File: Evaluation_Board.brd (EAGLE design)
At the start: 60.9 x 39.4 mm, 41 parts, among them IC1 MEGA32-A, IC2 FT232RL, IC3 317EMP, J1 DCJ0202

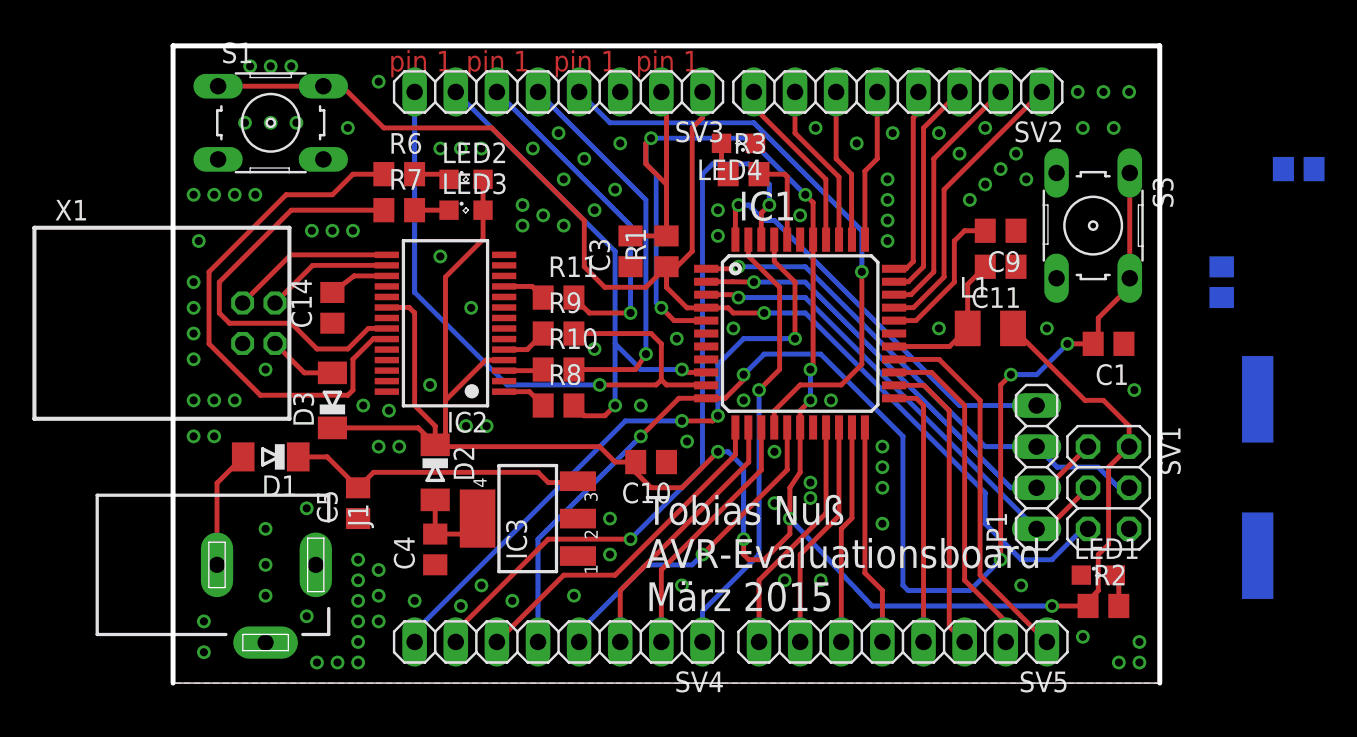
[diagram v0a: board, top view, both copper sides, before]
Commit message: Quarz eingefügt
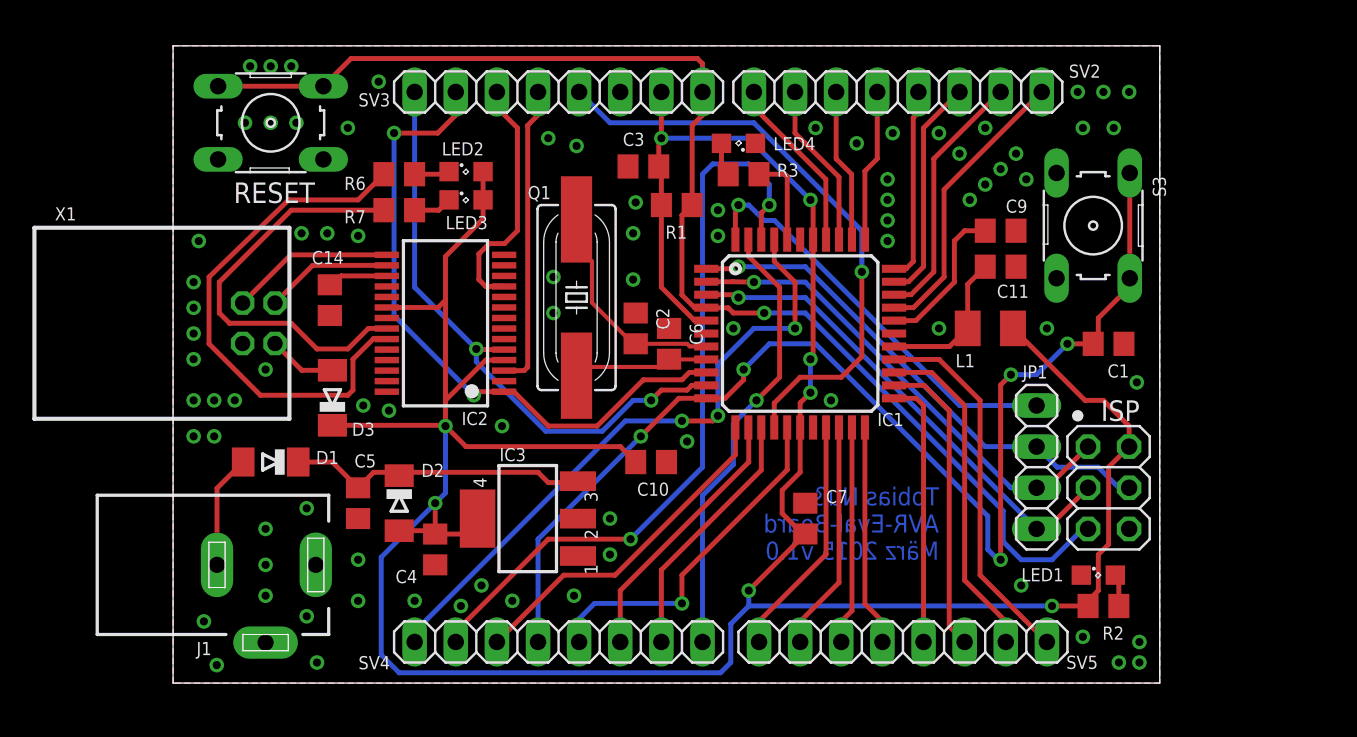
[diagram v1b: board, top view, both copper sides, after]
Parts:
- removed R10, R11, R8, R9: 1k, rcl:R0805
- added C7: 100n, rcl:C0805
- C2, C6: value 100n -> 12p
- Q1: value (none) -> 16 MHz
- moved Q1 43.5 mm to (24.9, 23.8), flipped to the top
- moved C6 40.4 mm to (30.6, 21.0), flipped to the top, turned to 270 degrees
- moved C2 36.3 mm to (28.6, 21.9), flipped to the top
- moved C3 5.30 mm to (29.1, 31.9), turned to 0 degrees
- moved D2 2.93 mm to (14.0, 11.1)
- moved R1 2.93 mm to (31.1, 29.5), turned to 180 degrees
- moved LED3 0.63 mm to (18.1, 29.8)
- moved C14 0.50 mm to (9.68, 23.7)
- moved LED2 0.48 mm to (18.1, 31.6)
- moved D1 0.32 mm to (6.03, 13.7)
- moved D3 0.16 mm to (9.84, 17.6)
- renumbered S1 to RESET, SV1 to ISP
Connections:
- removed net N$2: C4.2, D2.A, IC3.4
- removed net N$21: IC2.1, R8.1
- removed net N$22: IC2.5, R9.1
- removed net N$23: IC2.3, R10.1
- removed net N$24: IC2.11, R11.1
- new net N$17: C2.2, IC1.7, Q1.2
- new net N$25: C6.2, IC1.8, Q1.1
- net +5V: now also C4.2, C7.2, D2.A, IC3.4; no longer D2.C
- net CTS: now also IC2.11; no longer R11.2
- net GND: now also C2.1, C6.1, C7.1
- net NETZ: now also D2.C
- net RTS: now also IC2.3; no longer R10.2
- net RX_USB: now also IC2.1; no longer R8.2
- net TX_USB: now also IC2.5; no longer R9.2
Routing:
- net +5V: track 174.9 -> 191.8 mm, vias 9 -> 8
- net N$17: track 0.00 -> 13.9 mm
- net N$25: track 0.00 -> 8.82 mm
- net RX_USB: track 32.9 -> 40.6 mm
- net CTS: track 21.0 -> 15.4 mm, vias 1 -> 0
- net N$2: track 5.12 -> 0.00 mm
- net RTS: track 23.9 -> 18.8 mm, vias 1 -> 0
- net PD2_INT0: track 81.1 -> 76.1 mm
- net RESET: track 83.3 -> 79.3 mm
- net TX_USB: track 40.9 -> 37.4 mm, vias 1 -> 2
- net N$22: track 2.82 -> 0.00 mm
- net N$21: track 2.76 -> 0.00 mm
- net N$24: track 2.69 -> 0.00 mm
- net N$23: track 2.44 -> 0.00 mm
- net OC2: track 20.2 -> 21.7 mm
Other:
- board text added: "Tobias Nuß AVR-Eval-Board März 2015 v1.0"
- board text removed: "Tobias Nuß AVR-Evaluationsboard März 2015"
- board text removed: "pin 1"

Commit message: Test mit einem neuen Branch namens edit.
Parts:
- removed C7: 100n, rcl:C0805
- added R10, R11, R8, R9: 1k, rcl:R0805
- C2, C6: value 12p -> 100n
- Q1: value 16 MHz -> (none)
- moved Q1 43.5 mm to (67.0, 12.7), flipped to the bottom
- moved C6 40.4 mm to (69.5, 31.8), flipped to the bottom, turned to 180 degrees
- moved C2 36.3 mm to (64.8, 24.8), flipped to the bottom
- moved C3 5.30 mm to (28.3, 26.7), turned to 90 degrees
- moved D2 2.93 mm to (16.2, 13.0)
- moved R1 2.93 mm to (30.5, 26.7), turned to 90 degrees
- moved LED3 0.63 mm to (18.1, 29.2)
- moved C14 0.50 mm to (9.84, 23.2)
- moved LED2 0.48 mm to (18.1, 31.1)
- moved D1 0.32 mm to (6.03, 14.0)
- moved D3 0.16 mm to (9.84, 17.5)
- renumbered ISP to SV1, RESET to S1
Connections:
- removed net N$17: C2.2, IC1.7, Q1.2
- removed net N$25: C6.2, IC1.8, Q1.1
- new net N$2: C4.2, D2.A, IC3.4
- new net N$21: IC2.1, R8.1
- new net N$22: IC2.5, R9.1
- new net N$23: IC2.3, R10.1
- new net N$24: IC2.11, R11.1
- net +5V: now also D2.C; no longer C4.2, C7.2, D2.A, IC3.4
- net CTS: now also R11.2; no longer IC2.11
- net GND: no longer C2.1, C6.1, C7.1
- net NETZ: no longer D2.C
- net RTS: now also R10.2; no longer IC2.3
- net RX_USB: now also R8.2; no longer IC2.1
- net TX_USB: now also R9.2; no longer IC2.5
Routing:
- net +5V: track 191.8 -> 174.9 mm, vias 8 -> 9
- net N$17: track 13.9 -> 0.00 mm
- net N$25: track 8.82 -> 0.00 mm
- net RX_USB: track 40.6 -> 32.9 mm
- net CTS: track 15.4 -> 21.0 mm, vias 0 -> 1
- net N$2: track 0.00 -> 5.12 mm
- net RTS: track 18.8 -> 23.9 mm, vias 0 -> 1
- net PD2_INT0: track 76.1 -> 81.1 mm
- net RESET: track 79.3 -> 83.3 mm
- net TX_USB: track 37.4 -> 40.9 mm, vias 2 -> 1
- net N$22: track 0.00 -> 2.82 mm
- net N$21: track 0.00 -> 2.76 mm
- net N$24: track 0.00 -> 2.69 mm
- net N$23: track 0.00 -> 2.44 mm
- net OC2: track 21.7 -> 20.2 mm
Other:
- board text added: "Tobias Nuß AVR-Evaluationsboard März 2015"
- board text added: "pin 1"
- board text removed: "Tobias Nuß AVR-Eval-Board März 2015 v1.0"
